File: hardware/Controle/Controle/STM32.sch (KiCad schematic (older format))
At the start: 13 parts, among them U501 STM32F103C8Tx, Y501 8mhz

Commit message: adicionado o TL7726 e modificada a placa
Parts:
- JP501: footprint Jumper:SolderJumper-3_P1.3mm_Open_Pad1.0x1.5mm -> Jumper:SolderJumper-3_P1.3mm_Open_RoundedPad1.0x1.5mm
- Y501: footprint Crystal:Crystal_HC49-U_Vertical -> Crystal:Crystal_SMD_HC49-SD
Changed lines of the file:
@@
 F 0 "JP501" V 4096 2552 50  0000 L CNN
 F 1 "Jumper_NC_Dual" V 4005 2552 50  0000 L CNN
-F 2 "Jumper:SolderJumper-3_P1.3mm_Open_Pad1.0x1.5mm" H 4050 2450 50  0001 C CNN
+F 2 "Jumper:SolderJumper-3_P1.3mm_Open_RoundedPad1.0x1.5mm" H 4050 2450 50  0001 C CNN
 F 3 "~" H 4050 2450 50  0001 C CNN
 	1    4050 2450
@@
 F 0 "Y501" V 4654 2831 50  0000 L CNN
 F 1 "8mhz" V 4745 2831 50  0000 L CNN
-F 2 "Crystal:Crystal_HC49-U_Vertical" H 4700 2700 50  0001 C CNN
+F 2 "Crystal:Crystal_SMD_HC49-SD" H 4700 2700 50  0001 C CNN
 F 3 "~" H 4700 2700 50  0001 C CNN
 	1    4700 2700

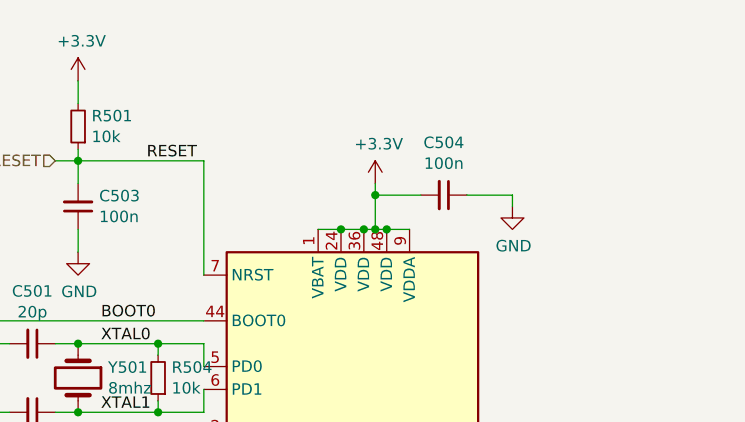
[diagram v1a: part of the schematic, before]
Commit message: control PCB updated
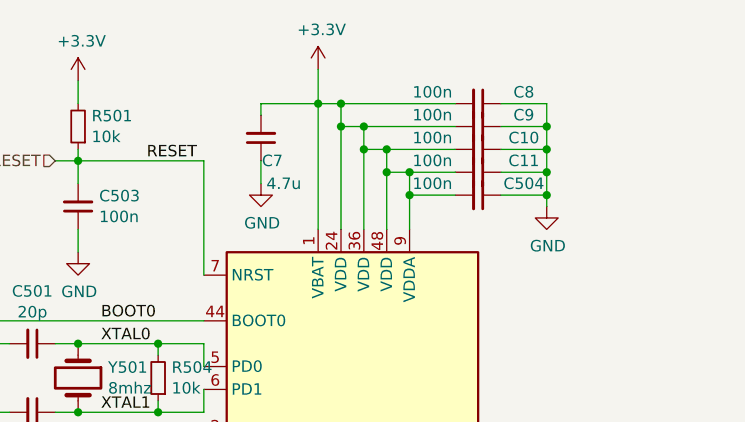
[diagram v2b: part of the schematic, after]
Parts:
- added C10, C11, C8, C9: 100n, Capacitor_SMD:C_0603_1608Metric_Pad1.08x0.95mm_HandSolder, symbol Device:C_Small
- added C7: 4.7u, Capacitor_SMD:C_1210_3225Metric_Pad1.33x2.70mm_HandSolder, symbol Device:C_Small
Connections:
- net +3V3: now also C10.2, C11.2, C7.2, C8.2, C9.2
- net GND: now also C10.1, C11.1, C7.1, C8.1, C9.1
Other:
- moved on the sheet: C504
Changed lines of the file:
@@
 $EndDescr
 $Comp
-L power:+3.3V #PWR?
-U 1 1 60747711
-P 6000 1850
-AR Path="/60747711" Ref="#PWR?"  Part="1"
-AR Path="/607427E0/60747711" Ref="#PWR0508"  Part="1"
-F 0 "#PWR0508" H 6000 1700 50  0001 C CNN
-F 1 "+3.3V" H 6015 2023 50  0000 C CNN
-F 2 "" H 6000 1850 50  0001 C CNN
-F 3 "" H 6000 1850 50  0001 C CNN
-	1    6000 1850
-	1    0    0    -1
-$EndComp
-Connection ~ 6000 2050
-$Comp
-L Device:C_Small C?
-U 1 1 60747718
-P 6300 1900
-AR Path="/60747718" Ref="C?"  Part="1"
-AR Path="/607427E0/60747718" Ref="C504"  Part="1"
-F 0 "C504" V 6071 1900 50  0000 C CNN
-F 1 "100n" V 6162 1900 50  0000 C CNN
-F 2 "Capacitor_SMD:C_0603_1608Metric_Pad1.08x0.95mm_HandSolder" H 6300 1900 50  0001 C CNN
-F 3 "~" H 6300 1900 50  0001 C CNN
-	1    6300 1900
-	0    1    1    0
-$EndComp
-Wire Wire Line
-	6200 1900 6000 1900
-Wire Wire Line
-	6000 1850 6000 1900
-Connection ~ 6000 1900
-Wire Wire Line
-	6000 1900 6000 2050
-$Comp
 L power:GND #PWR?
 U 1 1 60747722
-P 6600 1950
+P 6750 1950
 AR Path="/60747722" Ref="#PWR?"  Part="1"
 AR Path="/607427E0/60747722" Ref="#PWR0509"  Part="1"
-F 0 "#PWR0509" H 6600 1700 50  0001 C CNN
-F 1 "GND" H 6605 1777 50  0000 C CNN
-F 2 "" H 6600 1950 50  0001 C CNN
-F 3 "" H 6600 1950 50  0001 C CNN
-	1    6600 1950
-	1    0    0    -1
-$EndComp
-Wire Wire Line
-	6600 1950 6600 1900
-Wire Wire Line
-	6600 1900 6400 1900
+F 0 "#PWR0509" H 6750 1700 50  0001 C CNN
+F 1 "GND" H 6755 1777 50  0000 C CNN
+F 2 "" H 6750 1950 50  0001 C CNN
+F 3 "" H 6750 1950 50  0001 C CNN
+	1    6750 1950
+	1    0    0    -1
+$EndComp
+Wire Wire Line
+	6750 1950 6750 1900
+Wire Wire Line
+	6750 1900 6550 1900
 Text Label 7000 4550 2    50   ~ 0
 CAN_TX
@@
 	5900 5350 5900 5050
 Connection ~ 5900 5050
-Wire Wire Line
-	5950 5050 5900 5050
-Wire Wire Line
-	6050 5050 5950 5050
-Connection ~ 5950 5050
-Wire Wire Line
-	5850 5050 5750 5050
-Wire Wire Line
-	5900 5050 5850 5050
-Connection ~ 5850 5050
-Wire Wire Line
-	6050 2050 6000 2050
-Wire Wire Line
-	6150 2050 6050 2050
-Connection ~ 6050 2050
-Wire Wire Line
-	6000 2050 5950 2050
-Connection ~ 5950 2050
-$Comp
-L MCU_ST_STM32F1:STM32F103C8Tx U?
-U 1 1 60747742
-P 5950 3550
-AR Path="/60747742" Ref="U?"  Part="1"
-AR Path="/607427E0/60747742" Ref="U501"  Part="1"
-F 0 "U501" H 5900 1961 50  0000 C CNN
-F 1 "STM32F103C8Tx" H 5900 1870 50  0000 C CNN
-F 2 "Package_QFP:LQFP-48_7x7mm_P0.5mm" H 5350 2150 50  0001 R CNN
-F 3 "http://www.st.com/st-web-ui/static/active/en/resource/technical/document/datasheet/CD00161566.pdf" H 5950 3550 50  0001 C CNN
-	1    5950 3550
-	1    0    0    -1
-$EndComp
 Text HLabel 7000 4450 2    50   Input ~ 0
 CAN_RX
@@
 Wire Wire Line
 	4500 3900 4650 3900
-Wire Wire Line
-	5750 2050 5850 2050
-Connection ~ 5850 2050
-Wire Wire Line
-	5850 2050 5950 2050
 $Comp
 L Device:Jumper_NC_Dual JP501
@@
 Wire Wire Line
 	5100 3550 5250 3550
+$Comp
+L power:+3.3V #PWR?
+U 1 1 60747711
+P 5750 1350
+AR Path="/60747711" Ref="#PWR?"  Part="1"
+AR Path="/607427E0/60747711" Ref="#PWR0508"  Part="1"
+F 0 "#PWR0508" H 5750 1200 50  0001 C CNN
+F 1 "+3.3V" H 5765 1523 50  0000 C CNN
+F 2 "" H 5750 1350 50  0001 C CNN
+F 3 "" H 5750 1350 50  0001 C CNN
+	1    5750 1350
+	1    0    0    -1
+$EndComp
+Wire Wire Line
+	6350 1900 6150 1900
+Wire Wire Line
+	6150 1900 6150 2050
+Wire Wire Line
+	6050 5050 5950 5050
+Wire Wire Line
+	5950 5050 5900 5050
+Connection ~ 5950 5050
+Wire Wire Line
+	5900 5050 5850 5050
+Wire Wire Line
+	5850 5050 5750 5050
+Connection ~ 5850 5050
+$Comp
+L MCU_ST_STM32F1:STM32F103C8Tx U?
+U 1 1 60747742
+P 5950 3550
+AR Path="/60747742" Ref="U?"  Part="1"
+AR Path="/607427E0/60747742" Ref="U501"  Part="1"
+F 0 "U501" H 5900 1961 50  0000 C CNN
+F 1 "STM32F103C8Tx" H 5900 1870 50  0000 C CNN
+F 2 "Package_QFP:LQFP-48_7x7mm_P0.5mm" H 5350 2150 50  0001 R CNN
+F 3 "http://www.st.com/st-web-ui/static/active/en/resource/technical/document/datasheet/CD00161566.pdf" H 5950 3550 50  0001 C CNN
+	1    5950 3550
+	1    0    0    -1
+$EndComp
+$Comp
+L Device:C_Small C?
+U 1 1 60747718
+P 6450 1900
+AR Path="/60747718" Ref="C?"  Part="1"
+AR Path="/607427E0/60747718" Ref="C504"  Part="1"
+F 0 "C504" V 6400 2100 50  0000 C CNN
+F 1 "100n" V 6400 1700 50  0000 C CNN
+F 2 "Capacitor_SMD:C_0603_1608Metric_Pad1.08x0.95mm_HandSolder" H 6450 1900 50  0001 C CNN
+F 3 "~" H 6450 1900 50  0001 C CNN
+	1    6450 1900
+	0    1    1    0
+$EndComp
+$Comp
+L Device:C_Small C?
+U 1 1 60714BEE
+P 6450 1800
+AR Path="/60714BEE" Ref="C?"  Part="1"
+AR Path="/607427E0/60714BEE" Ref="C11"  Part="1"
+F 0 "C11" V 6400 2000 50  0000 C CNN
+F 1 "100n" V 6400 1600 50  0000 C CNN
+F 2 "Capacitor_SMD:C_0603_1608Metric_Pad1.08x0.95mm_HandSolder" H 6450 1800 50  0001 C CNN
+F 3 "~" H 6450 1800 50  0001 C CNN
+	1    6450 1800
+	0    1    1    0
+$EndComp
+$Comp
+L Device:C_Small C?
+U 1 1 60715125
+P 6450 1700
+AR Path="/60715125" Ref="C?"  Part="1"
+AR Path="/607427E0/60715125" Ref="C10"  Part="1"
+F 0 "C10" V 6400 1900 50  0000 C CNN
+F 1 "100n" V 6400 1500 50  0000 C CNN
+F 2 "Capacitor_SMD:C_0603_1608Metric_Pad1.08x0.95mm_HandSolder" H 6450 1700 50  0001 C CNN
+F 3 "~" H 6450 1700 50  0001 C CNN
+	1    6450 1700
+	0    1    1    0
+$EndComp
+$Comp
+L Device:C_Small C?
+U 1 1 60715682
+P 6450 1600
+AR Path="/60715682" Ref="C?"  Part="1"
+AR Path="/607427E0/60715682" Ref="C9"  Part="1"
+F 0 "C9" V 6400 1800 50  0000 C CNN
+F 1 "100n" V 6400 1400 50  0000 C CNN
+F 2 "Capacitor_SMD:C_0603_1608Metric_Pad1.08x0.95mm_HandSolder" H 6450 1600 50  0001 C CNN
+F 3 "~" H 6450 1600 50  0001 C CNN
+	1    6450 1600
+	0    1    1    0
+$EndComp
+Wire Wire Line
+	6350 1800 6150 1800
+Wire Wire Line
+	6050 1800 6050 2050
+Wire Wire Line
+	6350 1700 6050 1700
+Wire Wire Line
+	5950 1700 5950 2050
+Wire Wire Line
+	6350 1600 5950 1600
+Wire Wire Line
+	5850 1600 5850 2050
+$Comp
+L Device:C_Small C?
+U 1 1 6071A30B
+P 6450 1500
+AR Path="/6071A30B" Ref="C?"  Part="1"
+AR Path="/607427E0/6071A30B" Ref="C8"  Part="1"
+F 0 "C8" V 6400 1700 50  0000 C CNN
+F 1 "100n" V 6400 1300 50  0000 C CNN
+F 2 "Capacitor_SMD:C_0603_1608Metric_Pad1.08x0.95mm_HandSolder" H 6450 1500 50  0001 C CNN
+F 3 "~" H 6450 1500 50  0001 C CNN
+	1    6450 1500
+	0    1    1    0
+$EndComp
+Wire Wire Line
+	6350 1500 5850 1500
+Wire Wire Line
+	5750 1500 5750 2050
+Wire Wire Line
+	5750 1350 5750 1500
+Connection ~ 5750 1500
+Wire Wire Line
+	5850 1600 5850 1500
+Connection ~ 5850 1600
+Connection ~ 5850 1500
+Wire Wire Line
+	5850 1500 5750 1500
+Wire Wire Line
+	5950 1700 5950 1600
+Connection ~ 5950 1700
+Connection ~ 5950 1600
+Wire Wire Line
+	5950 1600 5850 1600
+Wire Wire Line
+	6050 1800 6050 1700
+Connection ~ 6050 1800
+Connection ~ 6050 1700
+Wire Wire Line
+	6050 1700 5950 1700
+Wire Wire Line
+	6150 1900 6150 1800
+Connection ~ 6150 1900
+Connection ~ 6150 1800
+Wire Wire Line
+	6150 1800 6050 1800
+Wire Wire Line
+	6550 1500 6750 1500
+Wire Wire Line
+	6750 1500 6750 1600
+Connection ~ 6750 1900
+Wire Wire Line
+	6550 1600 6750 1600
+Connection ~ 6750 1600
+Wire Wire Line
+	6750 1600 6750 1700
+Wire Wire Line
+	6550 1700 6750 1700
+Connection ~ 6750 1700
+Wire Wire Line
+	6750 1700 6750 1800
+Wire Wire Line
+	6550 1800 6750 1800
+Connection ~ 6750 1800
+Wire Wire Line
+	6750 1800 6750 1900
+$Comp
+L Device:C_Small C?
+U 1 1 60736FEA
+P 5500 1650
+AR Path="/60736FEA" Ref="C?"  Part="1"
+AR Path="/607427E0/60736FEA" Ref="C7"  Part="1"
+F 0 "C7" H 5450 1750 50  0000 C CNN
+F 1 "4.7u" H 5400 1850 50  0000 C CNN
+F 2 "Capacitor_SMD:C_1210_3225Metric_Pad1.33x2.70mm_HandSolder" H 5500 1650 50  0001 C CNN
+F 3 "~" H 5500 1650 50  0001 C CNN
+	1    5500 1650
+	-1   0    0    1
+$EndComp
+Wire Wire Line
+	5500 1550 5500 1500
+Wire Wire Line
+	5500 1500 5750 1500
+$Comp
+L power:GND #PWR?
+U 1 1 60739C07
+P 5500 1850
+AR Path="/60739C07" Ref="#PWR?"  Part="1"
+AR Path="/607427E0/60739C07" Ref="#PWR0123"  Part="1"
+F 0 "#PWR0123" H 5500 1600 50  0001 C CNN
+F 1 "GND" H 5505 1677 50  0000 C CNN
+F 2 "" H 5500 1850 50  0001 C CNN
+F 3 "" H 5500 1850 50  0001 C CNN
+	1    5500 1850
+	1    0    0    -1
+$EndComp
+Wire Wire Line
+	5500 1850 5500 1750
 $EndSCHEMATC

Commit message: Update Controle PCB
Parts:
- removed C501, C502: 20p, Capacitor_SMD:C_0603_1608Metric_Pad1.08x0.95mm_HandSolder, symbol Device:C_Small
- removed R504: 10k, Resistor_SMD:R_0603_1608Metric_Pad0.98x0.95mm_HandSolder, symbol Device:R_Small
- removed U501: STM32F103C8Tx, Package_QFP:LQFP-48_7x7mm_P0.5mm, symbol MCU_ST_STM32F1:STM32F103C8Tx
- removed Y501: 8mhz, Crystal:Crystal_SMD_HC49-SD, symbol Device:Crystal
- added U501: STM32G431CBT6, Package_QFP:LQFP-48_7x7mm_P0.5mm, symbol STM32G431C8T6:STM32G431CBT6
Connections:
- net +3V3: now also U501.1 (VBAT), U501.20 (VREF+), U501.21 (VDDA), U501.24 (VDD), U501.36 (VDD), U501.48 (VDD)
- net ADC1_IN0: now also U501.8 (PA0)
- net ADC1_IN1: now also U501.9 (PA1)
- net ADC1_IN2: now also U501.10 (PA2)
- net ADCX_IN3: now also U501.11 (PA3)
- net ADCX_IN4: now also U501.12 (PA4)
- net ADCX_IN5: now also U501.13 (PA5)
- net BOOT0: now also U501.45 (PB8-BOOT0)
- net CAN_RX: now also U501.33 (PA11)
- net CAN_TX: now also U501.34 (PA12)
- net FAN: now also U501.32 (PA10)
- net GND: now also U501.19 (VSSA), U501.23 (VSS), U501.35 (VSS), U501.47 (VSS)
- net LED0: now also U501.3 (PC14-OSC32_IN)
- net LED1: now also U501.4 (PC15-OSC32_OUT)
- net RESET: now also U501.7 (PG10/~RST~)
- net SWCLK: now also U501.38 (PA14)
- net SWDIO: now also U501.37 (PA13)
- net TIM1_CH1: now also U501.30 (PA8)
- net TIM1_CH1N: now also U501.27 (PB13)
- net TIM1_CH2: now also U501.31 (PA9)
- net TIM1_CH2N: now also U501.28 (PB14)
- net USART3_RX: now also U501.44 (PB7)
- net USART3_TX: now also U501.43 (PB6)
- new net SWO: U501.40 (PB3)
- no-connect marks 15 -> 16
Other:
- moved on the sheet: C10, C11, C503, C504, C7, C8, C9, D501, D502, JP501, R501, R502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

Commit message: first version of layout
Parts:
- removed JP501: Jumper_NC_Dual, Jumper:SolderJumper-3_P1.3mm_Open_RoundedPad1.0x1.5mm, symbol Device:Jumper_NC_Dual
- added R504: BOOT0, Resistor_SMD:R_0402_1005Metric, symbol Device:R_Small
- added R505: 10k, Resistor_SMD:R_0603_1608Metric_Pad0.98x0.95mm_HandSolder, symbol Device:R_Small
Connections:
- net +3V3: now also R504.1
- net BOOT0: now also R504.2, R505.1
- net GND: now also R505.2
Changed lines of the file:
@@
 	7450 4200 7300 4200
-$Comp
-L Device:Jumper_NC_Dual JP501
-U 1 1 60782D59
-P 9700 3950
-F 0 "JP501" V 9746 4052 50  0000 L CNN
-F 1 "Jumper_NC_Dual" V 9655 4052 50  0000 L CNN
-F 2 "Jumper:SolderJumper-3_P1.3mm_Open_RoundedPad1.0x1.5mm" H 9700 3950 50  0001 C CNN
-F 3 "~" H 9700 3950 50  0001 C CNN
-	1    9700 3950
-	0    1    -1   0
-$EndComp
 $Comp
 L power:+3.3V #PWR?
@@
 	-1   0    0    -1
 $EndComp
-Wire Wire Line
-	9700 3650 9700 3700
 $Comp
 L power:GND #PWR?
@@
 $EndComp
 Wire Wire Line
-	9700 4250 9700 4200
-Wire Wire Line
 	7300 3750 7300 3950
 Text Label 7000 3750 2    50   ~ 0
@@
 Text HLabel 7150 2350 2    50   Input ~ 0
 USART3_TX
-Wire Wire Line
-	9600 3950 9050 3950
 Text HLabel 7150 3050 2    50   Output ~ 0
 TIM1_CH1N
@@
 L power:GND #PWR?
 U 1 1 60739C07
-P 2550 2400
+P 2550 2450
 AR Path="/60739C07" Ref="#PWR?"  Part="1"
 AR Path="/607427E0/60739C07" Ref="#PWR0123"  Part="1"
-F 0 "#PWR0123" H 2550 2150 50  0001 C CNN
-F 1 "GND" H 2555 2227 50  0000 C CNN
-F 2 "" H 2550 2400 50  0001 C CNN
-F 3 "" H 2550 2400 50  0001 C CNN
-	1    2550 2400
+F 0 "#PWR0123" H 2550 2200 50  0001 C CNN
+F 1 "GND" H 2555 2277 50  0000 C CNN
+F 2 "" H 2550 2450 50  0001 C CNN
+F 3 "" H 2550 2450 50  0001 C CNN
+	1    2550 2450
 	1    0    0    -1
 $EndComp
 Wire Wire Line
-	2550 2400 2550 2300
+	2550 2450 2550 2300
 Wire Wire Line
 	4600 3150 4100 3150
@@
 NoConn ~ 6700 2150
 NoConn ~ 6700 2250
+$Comp
+L Device:R_Small R505
+U 1 1 60A61AF0
+P 9700 4050
+F 0 "R505" V 9504 4050 50  0000 C CNN
+F 1 "10k" V 9595 4050 50  0000 C CNN
+F 2 "Resistor_SMD:R_0603_1608Metric_Pad0.98x0.95mm_HandSolder" H 9700 4050 50  0001 C CNN
+F 3 "~" H 9700 4050 50  0001 C CNN
+	1    9700 4050
+	-1   0    0    -1
+$EndComp
+Wire Wire Line
+	9050 3950 9700 3950
+Wire Wire Line
+	9700 4150 9700 4250
+$Comp
+L Device:R_Small R504
+U 1 1 60A66235
+P 9700 3850
+F 0 "R504" V 9500 3900 50  0000 C CNN
+F 1 "BOOT0" V 9600 3900 50  0000 C CNN
+F 2 "Resistor_SMD:R_0402_1005Metric" H 9700 3850 50  0001 C CNN
+F 3 "~" H 9700 3850 50  0001 C CNN
+	1    9700 3850
+	-1   0    0    -1
+$EndComp
+Connection ~ 9700 3950
+Wire Wire Line
+	9700 3650 9700 3750
 $EndSCHEMATC

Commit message: falta acabamento
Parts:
- C7: footprint Capacitor_SMD:C_1210_3225Metric_Pad1.33x2.70mm_HandSolder -> Capacitor_SMD:C_1206_3216Metric_Pad1.33x1.80mm_HandSolder
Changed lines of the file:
@@
 F 0 "C7" H 2500 2300 50  0000 C CNN
 F 1 "4.7u" H 2450 2400 50  0000 C CNN
-F 2 "Capacitor_SMD:C_1210_3225Metric_Pad1.33x2.70mm_HandSolder" H 2550 2200 50  0001 C CNN
+F 2 "Capacitor_SMD:C_1206_3216Metric_Pad1.33x1.80mm_HandSolder" H 2550 2200 50  0001 C CNN
 F 3 "~" H 2550 2200 50  0001 C CNN
 	1    2550 2200
